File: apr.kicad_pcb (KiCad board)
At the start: 2 copper layers, 95 parts, among them J1 Screw_Terminal_01x03, J10 Screw_Terminal_01x02, J11 Screw_Terminal_01x02, J12 Screw_Terminal_01x02, J13 Conn_01x04, J14 Conn_01x04, J15 Flash Module Conn, J16 Bateria Lítio 1, J17 Bateria Lítio 2, J18 LORA, J19 LORA, J2 Screw_Terminal_01x03, J20 Screw_Terminal_01x02, J21 Screw_Terminal_01x02, J22 Screw_Terminal_01x02, J23 Conn_01x20_Pin, J24 Conn_01x20_Pin, J25 Screw_Terminal_01x02, J26 Screw_Terminal_01x02, J27 Screw_Terminal_01x02, J28 Screw_Terminal_01x02, J29 A1, J3 Screw_Terminal_01x02, J30 Screw_Terminal_01x03, J31 Bateria Lítio 3, J32 Buzzer, J33 Bateria Lipo, J34 A2, J35 11, J36 12, J37 14, J4 Screw_Terminal_01x02, J5 Screw_Terminal_01x02, J6 Conn_01x20_Pin, J7 Conn_01x20_Pin, J8 Screw_Terminal_01x02, J9 Screw_Terminal_01x02, Q10 IRLZ34N, Q11 IRLZ34N, Q2 IRLZ34N, Q3 IRLZ34N, Q4 IRLZ34N, Q5 IRLZ34N, Q6 IRLZ34N, Q7 IRLZ34N, Q8 IRLZ34N, Q9 IRLZ34N, U3 LM7905_TO220

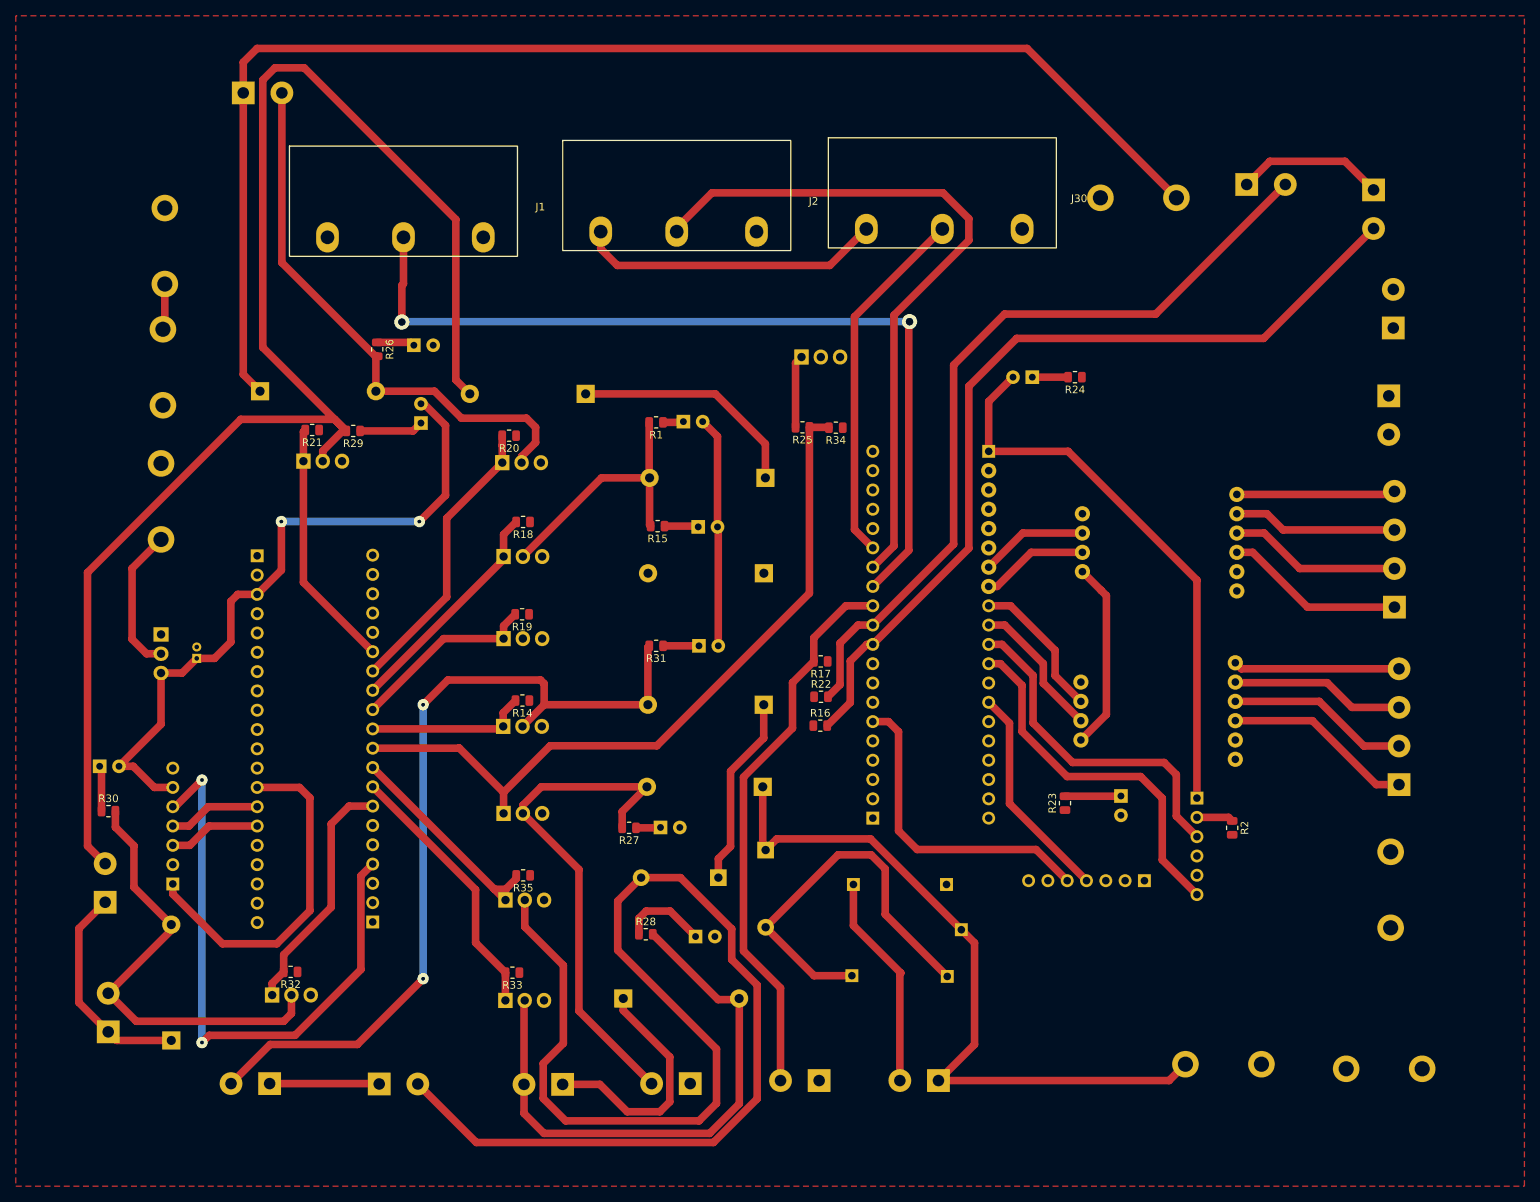
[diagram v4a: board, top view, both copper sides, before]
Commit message: Versão 1.0 placa híbrido - 1 camada
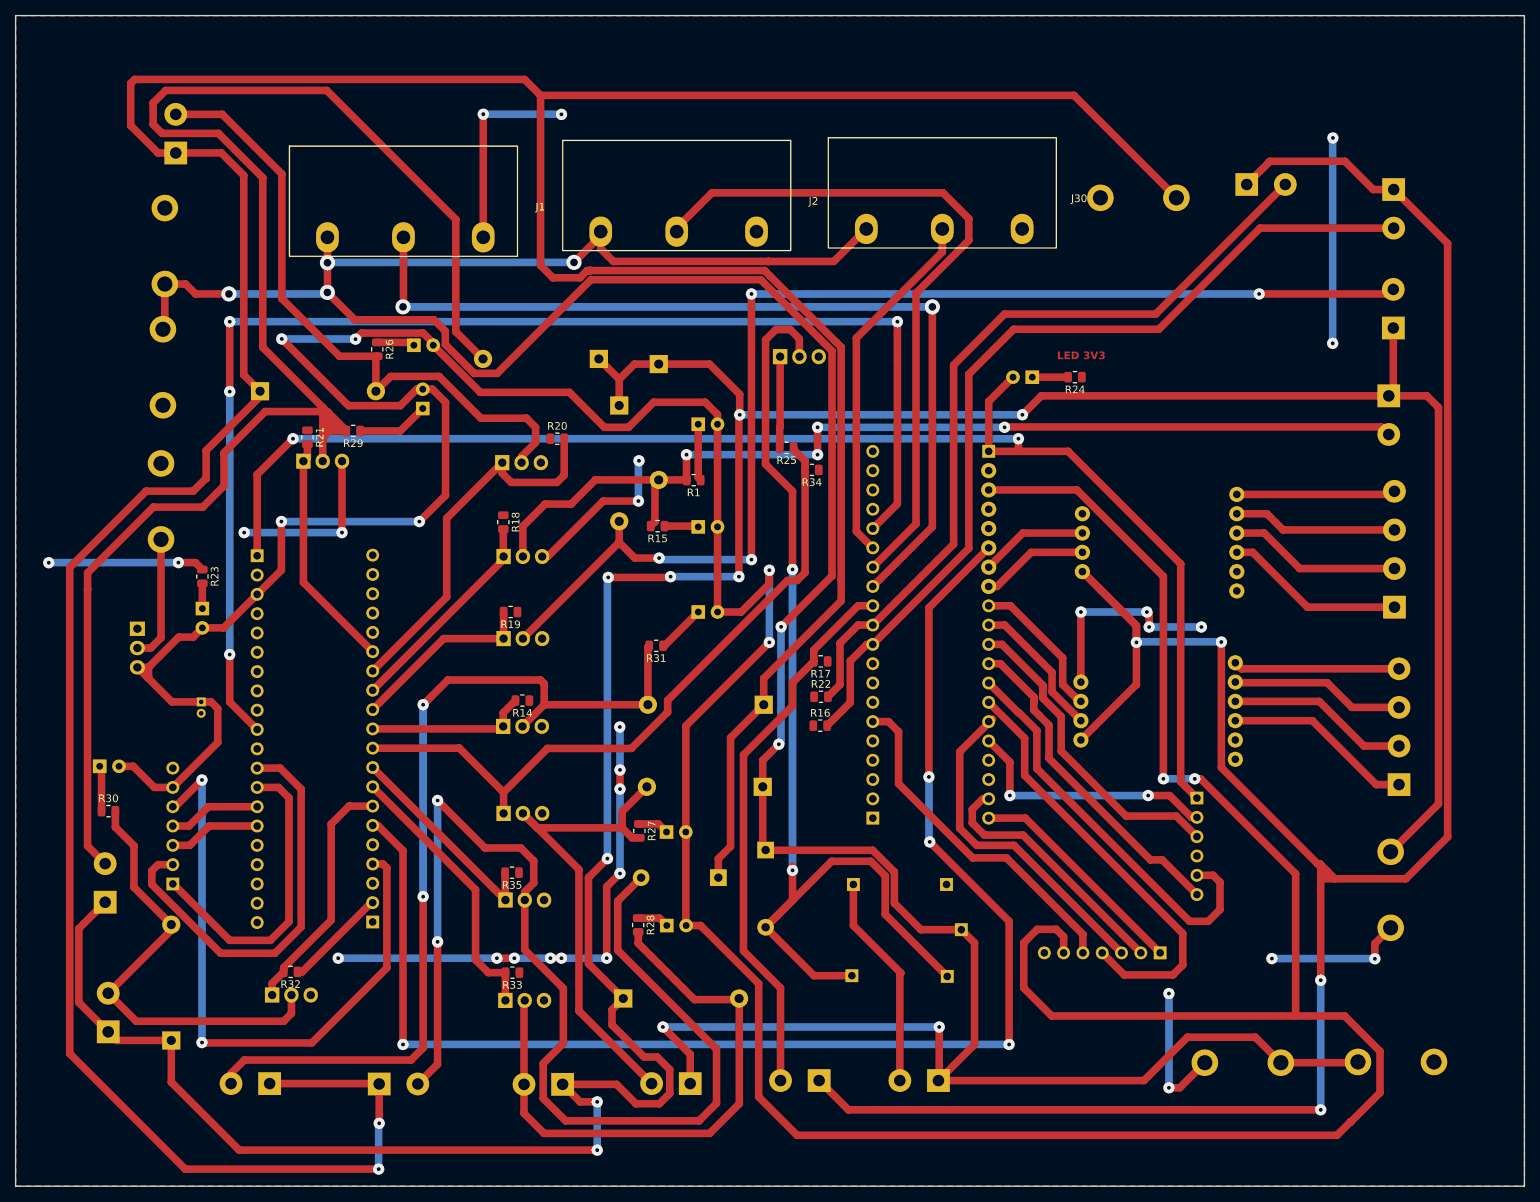
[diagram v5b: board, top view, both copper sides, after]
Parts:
- removed R2: 10k, Resistor_SMD:R_0805_2012Metric
- D10, D17, D18, D19, D20, D5, D6, D7: footprint LED_THT:LED_D3.0mm -> LED_THT:LED_D5.0mm
- moved D2 123.4 mm to (83.3, 95.5)
- moved R23 117.4 mm to (83.3, 91.3), turned to -90 degrees
- moved CR4 29.1 mm to (138.2, 68.8), turned to -90 degrees
- moved CR2 20.5 mm to (143.4, 63.4), turned to -90 degrees
- moved J10 11.9 mm to (79.8, 35.6), turned to 90 degrees
- moved J25 11.6 mm to (245.4, 155.2), turned to 180 degrees
- moved J19 9.72 mm to (209.4, 140.8)
- moved R1 9.07 mm to (148.0, 78.7)
- moved J31 7.45 mm to (215.2, 155.3), turned to 0 degrees
- moved R34 6.38 mm to (163.6, 77.3)
- moved R20 6.35 mm to (130.1, 73.2), turned to 0 degrees
- moved C1 5.76 mm to (83.2, 107.8), turned to -90 degrees
- moved CR5 4.92 mm to (135.5, 62.7)
- moved D20 4.45 mm to (148.6, 96.0)
- moved D17 4.05 mm to (144.5, 137.2)
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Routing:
- net +5V: track 120.8 -> 561.1 mm, vias 2 -> 8
- net +12L: track 92.0 -> 428.1 mm, vias 0 -> 8
- net +12C: track 215.5 -> 514.3 mm, vias 0 -> 2
- net +12V: track 141.9 -> 429.8 mm, vias 0 -> 8
- net +3.3V: track 44.4 -> 319.5 mm, vias 0 -> 4
- net GND: track 0.00 -> 261.6 mm, vias 0 -> 28
- net /SAVE_PB1: track 0.00 -> 183.6 mm, vias 0 -> 4
- net /RESET_PB3: track 0.00 -> 171.6 mm, vias 0 -> 4
- net /SUPER_CHARGE: track 0.00 -> 158.7 mm, vias 0 -> 4
- net +3V3: track 74.4 -> 189.0 mm, vias 0 -> 2
- net /PURGE_LINE: track 34.7 -> 134.4 mm, vias 0 -> 4
- net Net-(D4-A): track 52.0 -> 144.4 mm, vias 0 -> 2
- net /M1_PA12: track 0.00 -> 54.8 mm
- net /FLASH_SCK: track 0.00 -> 54.0 mm
- net /TX2_PA9: track 0.00 -> 44.2 mm
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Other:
- board outline added: 198.5 x 154 mm
- board text added: "LED 3V3"

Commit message: Primeiro commit nova versão
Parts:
- moved R34 2.50 mm to (163.6, 79.8)
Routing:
- net GND: track 261.6 -> 373.0 mm, vias 28 -> 34

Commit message: Esquemático e Layout PCB Sólido
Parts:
- removed CR2, CR3, CR4, CR5, CR6, CR7, CR8: UF4007-E3/73, Diode_THT:D_DO-15_P15.24mm_Horizontal
- removed D1: 1N4007, Diode_THT:D_DO-41_SOD81_P10.16mm_Horizontal
- removed D10, D17, D18, D19, D2, D20, D3: LED, LED_THT:LED_D5.0mm
- removed J1, J2: Screw_Terminal_01x03, Library:KT100-3PIN
- removed J10, J11, J12, J20, J21, J22, J3, J4, J5, J8, J9: Screw_Terminal_01x02, TerminalBlock:TerminalBlock_bornier-2_P5.08mm
- removed J14: Conn_01x04, TerminalBlock:TerminalBlock_bornier-4_P5.08mm
- removed J16: Bateria Lítio 1, Library:Screw Terminal 3D
- removed J17: Bateria Lítio 2, Library:Screw Terminal 3D
- removed J27, J28: Screw_Terminal_01x02, Library:Screw Terminal 3D
- removed J29: A1, Connector_PinHeader_2.54mm:PinHeader_1x01_P2.54mm_Vertical
- removed J34: A2, Connector_PinHeader_2.54mm:PinHeader_1x01_P2.54mm_Vertical
- removed J35: 11, Connector_PinHeader_2.54mm:PinHeader_1x01_P2.54mm_Vertical
- removed J36: 12, Connector_PinHeader_2.54mm:PinHeader_1x01_P2.54mm_Vertical
- removed J37: 14, Connector_PinHeader_2.54mm:PinHeader_1x01_P2.54mm_Vertical
- removed Q2, Q3, Q4, Q5, Q6, Q7, Q8, Q9: IRLZ34N, Package_TO_SOT_THT:TO-220-3_Vertical
- removed R1, R15, R23, R24, R29, R30, R31: 470, Resistor_SMD:R_0805_2012Metric
- removed R14, R18, R19, R20, R21, R32, R33, R34: 4K7, Resistor_SMD:R_0805_2012Metric
- removed R16: 5.6k, Resistor_SMD:R_0805_2012Metric
- removed R17: 270k, Resistor_SMD:R_0805_2012Metric
- removed R22: 390k, Resistor_SMD:R_0805_2012Metric
- added K1: Fujitsu_FTR-LYCA005x, Relay_THT:Relay_SPDT_Finder_36.11, B.Cu at (208.9, 51.1)
- CR1: footprint Diode_THT:D_DO-15_P15.24mm_Horizontal -> Diode_THT:D_A-405_P12.70mm_Horizontal
- J25: value Screw_Terminal_01x02 -> VSUPPLY TRANSDUCER
- J26: value Screw_Terminal_01x02 -> IGNITION; footprint TerminalBlock:TerminalBlock_bornier-2_P5.08mm -> Library:Screw Terminal 3D
- J30: moved to B.Cu
- J31: value Bateria Lítio 3 -> Bateria Lítio
- J32: footprint TerminalBlock:TerminalBlock_bornier-2_P5.08mm -> Library:Screw Terminal 3D
- U1: value ~ -> Ag9905LP; footprint Library:hx711 -> Converter_DCDC:Converter_DCDC_Silvertel_Ag99xxLP_THT
- moved J25 164.0 mm to (97.8, 83.8), turned to 90 degrees
- moved J13 153.0 mm to (89.8, 94.1), turned to -90 degrees
- moved J26 137.5 mm to (222.1, 83.3), turned to 90 degrees
- moved C1 125.7 mm to (208.5, 97.8)
- moved J33 122.7 mm to (196.3, 118.7), turned to 180 degrees
- moved J6 122.1 mm to (210.0, 73.1), turned to 90 degrees
- moved U3 120.5 mm to (195.3, 99.3), turned to 180 degrees
- moved U1 114.7 mm to (107.3, 56.7), turned to 90 degrees
- moved U2 113.6 mm to (105.7, 105.2), turned to 0 degrees
- moved J15 101.3 mm to (124.7, 73.0)
- moved D4 98.2 mm to (208.4, 43.4), turned to 180 degrees
- moved D6 92.5 mm to (233.2, 122.2), turned to 180 degrees
- moved R27 91.3 mm to (231.6, 114.8), turned to 0 degrees
- moved R35 90.9 mm to (178.8, 57.7)
- moved Q10 90.0 mm to (176.4, 61.4)
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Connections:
- net /TRANSDUCER_CAMARA_PA0 renamed /TRANSDUCER
- CR1 pad 1: +12C -> +12V
- CR1 pad 2: /QUICK_DISCONNECT -> /IGNITE
- D5 pad 2: +5V -> +3.3V
- D7 pad 2: +5V -> +3V3
- J23 pad 7: /DT2 -> unconnected-(J23-Pin_7-Pad7)
- J23 pad 8: /SCK2 -> unconnected-(J23-Pin_8-Pad8)
- J24 pad 10: /THERMISTOR_CAMARA -> unconnected-(J24-Pin_10-Pad10)
- J24 pad 11: /THERMISTOR_LINE -> unconnected-(J24-Pin_11-Pad11)
- J24 pad 12: /THERMISTOR_TANK -> unconnected-(J24-Pin_12-Pad12)
- J24 pad 13: /TRANSDUCER_LINE_PA2 -> unconnected-(J24-Pin_13-Pad13)
- J24 pad 14: /TRANSDUCER_TANK_PA1 -> unconnected-(J24-Pin_14-Pad14)
- J26 pad 1: +12C -> +12V
- J6 pad 11: /QUICK_DISCONNECT_PA4 -> unconnected-(J6-Pin_11-Pad11)
- J6 pad 12: /SUPER_CHARGE_PA3 -> unconnected-(J6-Pin_12-Pad12)
- J6 pad 13: /PURGE_LINE_PA2 -> unconnected-(J6-Pin_13-Pad13)
- J6 pad 14: /VENT_PA1 -> unconnected-(J6-Pin_14-Pad14)
- J6 pad 15: /FUEL_LINE_A0 -> unconnected-(J6-Pin_15-Pad15)
- J6 pad 7: /PURGE_TANK_PB0 -> unconnected-(J6-Pin_7-Pad7)
- J6 pad 8: /INJECTION_PA7 -> unconnected-(J6-Pin_8-Pad8)
- J7 pad 1: +3V3 -> +3.3V
- R26 pad 1: Net-(D7-K) -> GND
- R26 pad 2: /VENT -> Net-(D5-K)
- R27 pad 1: Net-(D10-K) -> GND
- R27 pad 2: /ARM -> Net-(D6-K)
- R28 pad 1: Net-(D17-K) -> GND
- R28 pad 2: /INJECTION -> Net-(D7-K)
- U1 pad 1: Net-(J14-Pin_4) -> unconnected-(U1-+VDC-Pad1)_1
- U1 pad 2: Net-(J14-Pin_3) -> unconnected-(U1-+VDC-Pad1)
- U1 pad 3: Net-(J14-Pin_2) -> unconnected-(U1--VDC-Pad3)
- U1 pad 4: Net-(J14-Pin_1) -> unconnected-(U1-ADJ-Pad4)
- U1 pad 7: +3.3V -> unconnected-(U1-VIN--Pad7)_1
- U1 pad 8: /SCK2 -> unconnected-(U1-VIN--Pad7)
- U2 pad 7: +3.3V -> +3V3
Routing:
- net +12C: track 514.3 -> 0.00 mm, vias 2 -> 0
- net +12L: track 428.1 -> 0.00 mm, vias 8 -> 0
- net GND: track 373.0 -> 54.9 mm, vias 34 -> 6
- net +3.3V: track 319.5 -> 5.56 mm, vias 4 -> 0
- net +5V: track 561.1 -> 322.9 mm, vias 8 -> 4
- net /FUEL_LINE: track 225.6 -> 0.00 mm
- net +12V: track 429.8 -> 228.5 mm, vias 8 -> 0
- net /SUPER_CHARGE: track 158.7 -> 0.00 mm, vias 4 -> 0
- net /PURGE_LINE: track 134.4 -> 0.00 mm, vias 4 -> 0
- net /RESET_PB3: track 171.6 -> 37.8 mm, vias 4 -> 2
- net +3V3: track 189.0 -> 62.1 mm
- net /QUICK_DISCONNECT: track 119.0 -> 0.00 mm, vias 2 -> 0
- net /TRANSDUCER_LINE_PA2: track 118.9 -> 0.00 mm, vias 2 -> 0
- net /THERMISTOR_CAMARA: track 118.3 -> 0.00 mm
- net Net-(D4-A): track 144.4 -> 29.5 mm, vias 2 -> 0
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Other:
- board size 198.5 x 154 mm -> 156.8 x 97 mm
- board text added: "+"
- board text added: "-"
- board text added: "BUZZER"
- board text added: "CONVERSOR"
- board text added: "IGNITE"
- board text added: "LED 3V3 TR"
- board text added: "LED 5V"
- board text added: "LIPO BAT"
- board text added: "LITIO BAT"
- board text added: "SOLID MOTOR INSTRUMENTATION PCB"
- board text added: "TRANS"
- board text added: "VSUPPLY TRANSD"
- board text removed: "LED 3V3"

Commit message: Layout Final
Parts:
- removed Q11: IRLZ34N, Package_TO_SOT_THT:TO-220-3_Vertical
- removed U1: Ag9905LP, Converter_DCDC:Converter_DCDC_Silvertel_Ag99xxLP_THT
- added CR2: UF4007-E3/73, Diode_THT:D_A-405_P12.70mm_Horizontal, B.Cu at (212.9, 44.6)
- added J27: ARM, Library:Screw Terminal 3D, B.Cu at (211.1, 33.8)
- added Q1: BC547, Package_TO_SOT_THT:TO-92_Inline, B.Cu at (237.9, 70.8)
- added Q12: IRLZ34N, Package_TO_SOT_THT:TO-220-3_Vertical, B.Cu at (209.0, 55.5)
- added R36: 4K7, Resistor_SMD:R_0805_2012Metric, F.Cu at (206.5, 61.7)
- moved J32 74.0 mm to (237.9, 33.6), turned to 180 degrees
- moved J26 61.9 mm to (185.1, 33.6), turned to 180 degrees
- moved R25 50.7 mm to (235.6, 76.0), turned to 0 degrees
- moved D5 49.4 mm to (153.0, 45.8), turned to 0 degrees
- moved CR1 46.2 mm to (186.2, 44.9)
- moved R26 44.0 mm to (152.9, 50.9), turned to 90 degrees
- moved J33 38.6 mm to (233.8, 109.0), turned to -90 degrees
- moved J31 34.1 mm to (234.0, 95.2), turned to 90 degrees
- moved R28 32.0 mm to (108.7, 66.2), turned to 0 degrees
- moved D4 29.2 mm to (227.9, 65.2), turned to 0 degrees
- moved D7 22.8 mm to (112.2, 62.2), turned to 0 degrees
- moved U3 21.7 mm to (209.3, 115.8), turned to 90 degrees
- moved C1 20.8 mm to (196.0, 114.5)
- moved K1 19.7 mm to (227.5, 57.5), turned to 0 degrees
- moved D6 19.5 mm to (231.0, 102.8)
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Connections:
- D5 pad 2: +3.3V -> +12V
- J19 pad 1: /M0_PB12 -> /M0_PB13
- J19 pad 2: /M1_PB13 -> /M1_PB12
- J23 pad 19: /M1_PB13 -> /M0_PB13
- J23 pad 20: /M0_PB12 -> /M1_PB12
- J23 pad 6: /SAVE_PB1 -> /SAVE_PA1
- J24 pad 10: unconnected-(J24-Pin_10-Pad10) -> GND
- J24 pad 11: unconnected-(J24-Pin_11-Pad11) -> GND
- J24 pad 12: unconnected-(J24-Pin_12-Pad12) -> GND
- J24 pad 13: unconnected-(J24-Pin_13-Pad13) -> GND
- J24 pad 14: unconnected-(J24-Pin_14-Pad14) -> GND
- J6 pad 1: unconnected-(J6-Pin_1-Pad1) -> +5V
- J6 pad 10: /ARM_PA5 -> /IGINTE_PA5
- J6 pad 15: unconnected-(J6-Pin_15-Pad15) -> /SAVE_PA1
- J6 pad 6: /SAVE_PB1 -> unconnected-(J6-Pin_6-Pad6)
- J6 pad 9: /IGNITE_PA6 -> /ARM_PA6
- J7 pad 3: +5V -> unconnected-(J7-Pin_3-Pad3)
- Q10 pad 1: /IGNITE_PA6 -> /IGINTE_PA5
- R25 pad 1: /ARM_PA5 -> /ARM_PA6
- R35 pad 2: /IGNITE_PA6 -> /IGINTE_PA5
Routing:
- net +12V: track 228.5 -> 334.1 mm
- net GND: track 54.9 -> 152.6 mm
- net /SAVE_PB1: track 74.9 -> 0.00 mm, vias 2 -> 0
- net /ARM_PA6: track 0.00 -> 67.1 mm
- net /SAVE_PA1: track 0.00 -> 57.7 mm, vias 0 -> 2
- net /ARM_PA5: track 46.7 -> 0.00 mm
- net Net-(J32-Pin_2): track 58.5 -> 11.9 mm
- net /IGNITE: track 54.1 -> 25.5 mm
- net /IGNITE_PA6: track 25.7 -> 0.00 mm
- net /ARM: track 0.00 -> 24.6 mm
- net /M1_PB13: track 23.5 -> 0.00 mm
- net /FLASH_SCK: track 45.6 -> 68.4 mm
- net /IGINTE_PA5: track 0.00 -> 21.7 mm
- net /FLASH_MISO: track 46.6 -> 66.7 mm
- net /FLASH_MOSI: track 39.6 -> 58.3 mm
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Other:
- board size 156.8 x 97 mm -> 180 x 115 mm
- board text added: "ARM"
- board text added: "LED 12V"
- board text added: "LED HX"
- board text removed: "-"
- board text removed: "LED 3V3 TR"
- board text removed: "LED 5V"
- board text removed: "LIPO BAT"
- board text removed: "LITIO BAT"
